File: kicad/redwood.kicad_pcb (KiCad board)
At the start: 2 copper layers, 136.6 x 97.9 mm, 39 parts, among them J1 Haptic, J2 TRRS, K1 diode-choc, K10 diode-choc, K11 diode-choc, K12 diode-choc, K13 diode-choc, K14 diode-choc, K15 diode-choc, K16 diode-choc, K17 diode-choc, K18 diode-choc, K19 diode-choc, K2 diode-choc, K20 choc_rotary, K21 diode-choc, K22 diode-choc, K23 diode-choc, K24 diode-choc, K3 diode-choc, K4 diode-choc, K5 diode-choc, K6 diode-choc, K7 diode-choc, K8 diode-choc, K9 diode-choc, SW1 Reset, U1 ProMicro_r

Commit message: - project updates from footprints
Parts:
- added V2: Via, mmccoyd:VIA-0.8mm, F.Cu at (182.0, 85.7)
- moved J1 0.50 mm to (215.5, 93.5)
- moved J2 0.50 mm to (214.5, 129.4)
- moved R1 0.50 mm to (221.1, 90.4)
- moved R2 0.50 mm to (221.1, 80.0)
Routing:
- net VCC: track 224.7 -> 225.9 mm
- net col1: track 196.3 -> 195.5 mm
- net SCL: track 41.6 -> 42.1 mm
- net SDA: track 42.3 -> 42.8 mm
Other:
- outline, holes or cut-outs redrawn

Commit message: Symbols and footprints all from project libs
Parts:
- V1, V2: footprint mmccoyd:VIA-0.8mm -> redwood:VIA-0.8mm

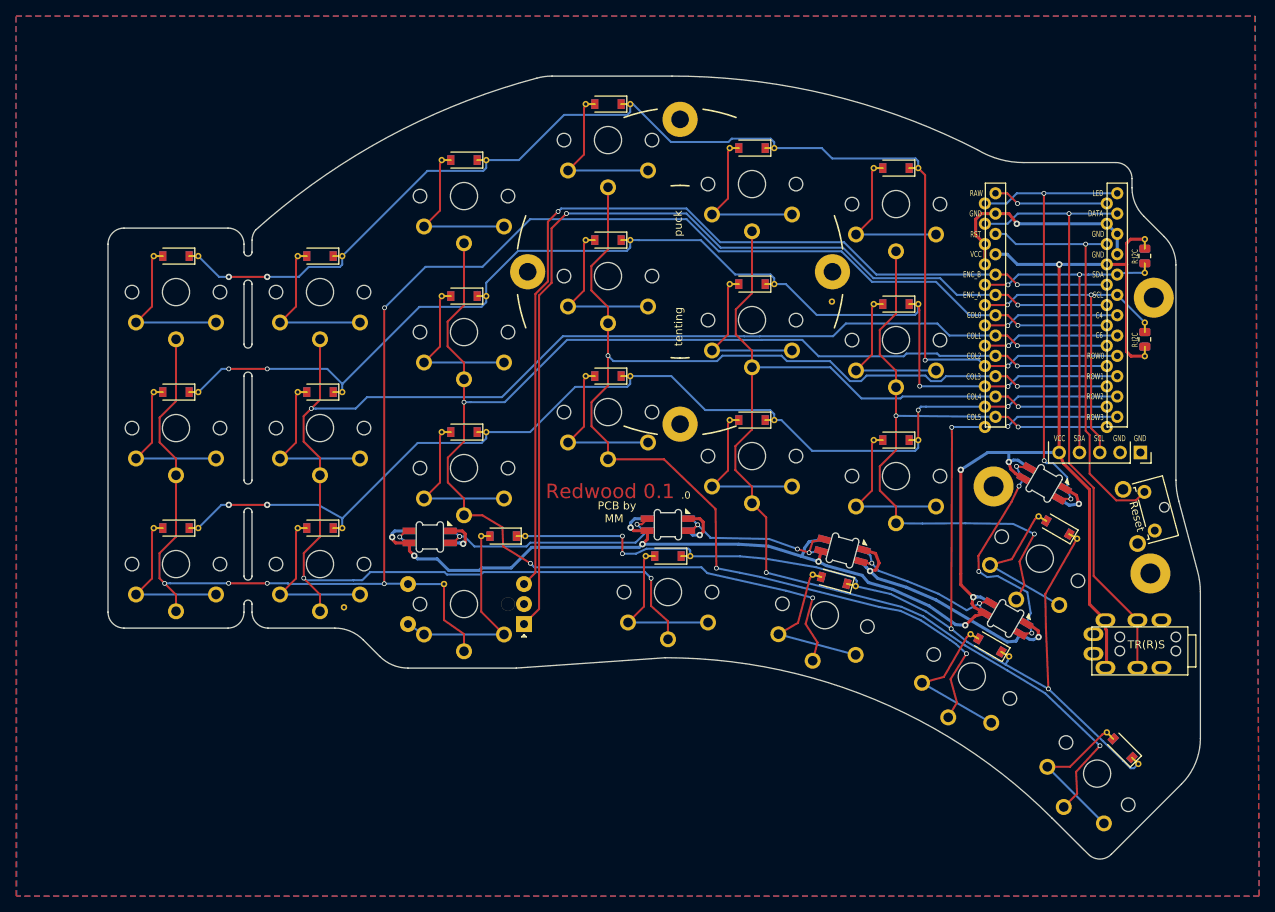
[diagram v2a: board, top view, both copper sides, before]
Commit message: Common cathode diodes reduce trace clutter
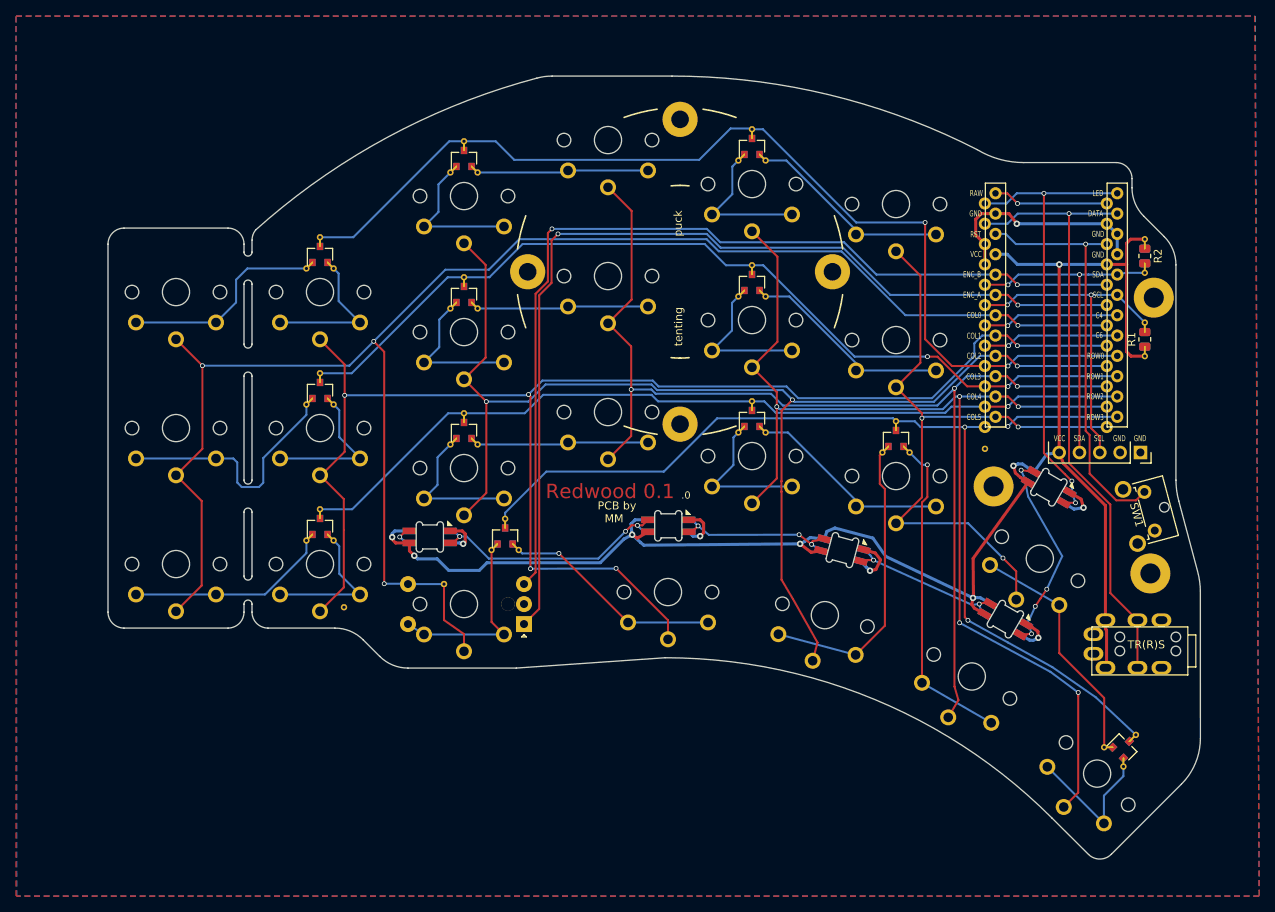
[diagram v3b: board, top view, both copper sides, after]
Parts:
- removed D6: Diode, redwood:D_SOD-123_rev
- added D10: BAV70, ki_syms:SOT-23, F.Cu at (118.0, 96.8)
- added D11: BAV70, ki_syms:SOT-23, F.Cu at (136.0, 84.8)
- added D12: BAV70, ki_syms:SOT-23, F.Cu at (172.0, 83.3)
- added D13: BAV70, ki_syms:SOT-23, F.Cu at (118.0, 113.8)
- added D14: BAV70, ki_syms:SOT-23, F.Cu at (136.0, 101.8)
- added D15: BAV70, ki_syms:SOT-23, F.Cu at (172.0, 100.3)
- added D16: BAV70, ki_syms:SOT-23, F.Cu at (141.1, 115.0)
- added D17: BAV70, ki_syms:SOT-23, F.Cu at (190.0, 102.8)
- added D18: BAV70, ki_syms:SOT-23, F.Cu at (218.5, 141.4)
- added D7: BAV70, ki_syms:SOT-23, F.Cu at (118.0, 79.8)
- added D8: BAV70, ki_syms:SOT-23, F.Cu at (136.0, 67.8)
- added D9: BAV70, ki_syms:SOT-23, F.Cu at (172.0, 66.3)
- D1, D2, D3, D4, D5: footprint redwood:SK6812-MINI-E -> ki_syms:SK6812-MINI-E
- K1, K10, K11, K12, K13, K14, K15, K16, K17, K18, K19, K2, K21, K22, K23, K24, K3, K4, K5, K6, K7, K8, K9: value diode-choc -> SW_Key; footprint redwood:pg1350-DR -> redwood:pg1350-R
- K20: value choc_rotary -> SW_Rotary
- R1, R2: footprint redwood:R_0805_2012Metric -> ki_syms:R_0805_2012Metric
- SW1: footprint redwood:SW_Tactile_SPST_Angled_MJTP1117 -> ki_syms:SW_Tactile_SPST_Angled_MJTP1117
- V1, V2: footprint redwood:VIA-0.8mm -> ki_syms:VIA-0.8mm
- moved V2 26.5 mm to (201.1, 104.1)
- moved K1 4.50 mm to (100.0, 84.5)
- moved K10 4.50 mm to (154.0, 82.5)
- moved K11 4.50 mm to (172.0, 88.0)
- moved K12 4.50 mm to (190.0, 90.5)
- moved K13 4.50 mm to (100.0, 118.5)
- moved K14 4.50 mm to (118.0, 118.5)
- moved K15 4.50 mm to (136.0, 106.5)
- moved K16 4.50 mm to (154.0, 99.5)
- moved K17 4.50 mm to (172.0, 105.0)
- moved K18 4.50 mm to (190.0, 107.5)
- moved K2 4.50 mm to (118.0, 84.5)
- moved K21 4.50 mm to (161.5, 122.0)
- moved K3 4.50 mm to (136.0, 72.5)
- moved K4 4.50 mm to (154.0, 65.5)
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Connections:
- K1 pad 2: row0 -> Net-(D7-Pad1)
- K10 pad 2: row1 -> Net-(D11-Pad2)
- K11 pad 2: row1 -> Net-(D12-Pad1)
- K12 pad 2: row1 -> Net-(D12-Pad2)
- K13 pad 2: row2 -> Net-(D13-Pad1)
- K14 pad 2: row2 -> Net-(D13-Pad2)
- K15 pad 2: row2 -> Net-(D14-Pad1)
- K16 pad 2: row2 -> Net-(D14-Pad2)
- K17 pad 2: row2 -> Net-(D15-Pad1)
- K18 pad 2: row2 -> Net-(D15-Pad2)
- K19 pad 2: row3 -> Net-(D18-Pad1)
- K2 pad 2: row0 -> Net-(D7-Pad2)
- K21 pad 2: row3 -> Net-(D16-Pad2)
- K22 pad 2: row3 -> Net-(D17-Pad1)
- K23 pad 2: row3 -> Net-(D17-Pad2)
- K24 pad 2: row3 -> Net-(D18-Pad2)
- K3 pad 2: row0 -> Net-(D8-Pad1)
- K4 pad 2: row0 -> Net-(D8-Pad2)
- K5 pad 2: row0 -> Net-(D9-Pad1)
- K6 pad 2: row0 -> Net-(D9-Pad2)
- K7 pad 2: row1 -> Net-(D10-Pad1)
- K8 pad 2: row1 -> Net-(D10-Pad2)
- K9 pad 2: row1 -> Net-(D11-Pad1)
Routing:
- net Net-(D17-Pad2): track 0.00 -> 30.4 mm, vias 0 -> 1
- net row1: track 143.9 -> 114.3 mm, vias 4 -> 2
- net row2: track 136.0 -> 107.4 mm, vias 4 -> 1
- net row0: track 156.8 -> 128.6 mm, vias 4 -> 2
- net Net-(D17-Pad1): track 0.00 -> 27.2 mm
- net col3: track 168.8 -> 142.7 mm, vias 4 -> 3
- net col2: track 178.9 -> 155.3 mm, vias 4 -> 3
- net row3: track 156.1 -> 133.0 mm, vias 6 -> 3
- net GND: track 76.8 -> 55.4 mm
- net Net-(D10-Pad1): track 0.00 -> 21.1 mm
- net Net-(D18-Pad1): track 0.00 -> 20.1 mm
- net Net-(D16-Pad2): track 0.00 -> 17.4 mm, vias 0 -> 1
- net Net-(D7-Pad1): track 0.00 -> 15.7 mm
- net Net-(D12-Pad2): track 0.00 -> 15.7 mm
- net Net-(D15-Pad2): track 0.00 -> 15.6 mm
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
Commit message: Battery support, Hillside logo, mounting holes
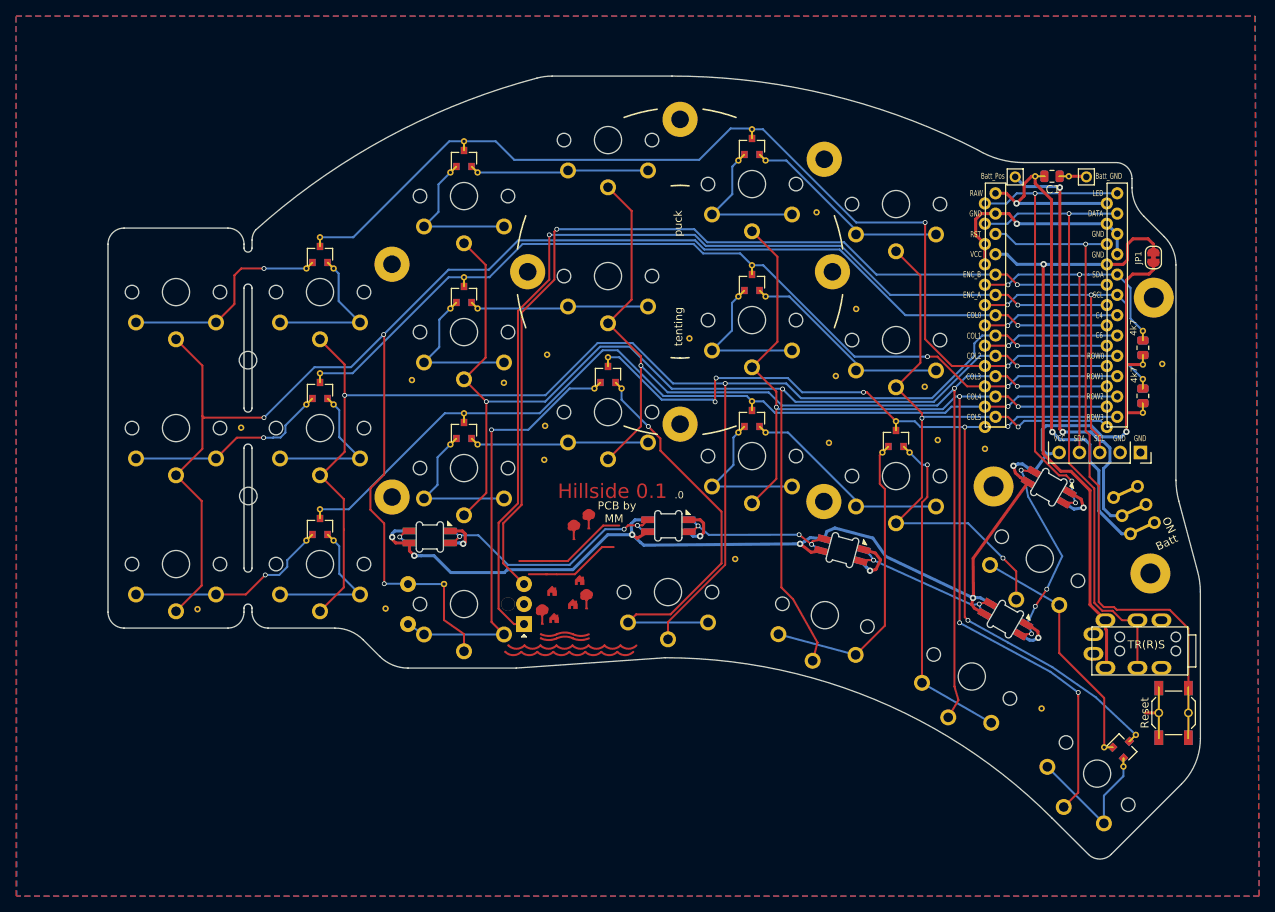
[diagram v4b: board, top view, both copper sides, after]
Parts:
- added C1: 4u7, ki_syms:C_0805_2012Metric, F.Cu at (209.5, 70.0)
- added H3: Scene, redwood:Hillside_Scene, F.Cu at (149.1, 121.4)
- added H4: MountHole, ki_mount_hole:MountingHole_2.2mm_M2_Pad, F.Cu at (127.0, 81.0)
- added H5: MountHole, ki_mount_hole:MountingHole_2.2mm_M2_Pad, F.Cu at (127.0, 110.1)
- added H6: MountHole, ki_mount_hole:MountingHole_2.2mm_M2, F.Cu at (109.0, 93.0)
- added H7: MountHole, ki_mount_hole:MountingHole_2.2mm_M2, F.Cu at (109.0, 110.0)
- added H8: MountHole, ki_mount_hole:MountingHole_2.2mm_M2_Pad, F.Cu at (181.0, 110.7)
- added H9: MountHole, ki_mount_hole:MountingHole_2.2mm_M2_Pad, F.Cu at (181.0, 67.9)
- added J3: Batt_Pos, ki_syms:1pin_conn, F.Cu at (204.9, 70.1)
- added J4: Batt_GND, ki_syms:1pin_conn, F.Cu at (213.8, 70.1)
- added JP1: SolderJumper_2_Bridged, ki_syms:SolderJumper-2_P1.3mm_Bridged_RoundedPad1.0x1.5mm, F.Cu at (222.2, 80.2)
- added SW2: SW_Power, ki_syms:SW_SPDT_JS202011AQN, F.Cu at (219.8, 111.8)
- added V10: Via, ki_syms:VIA-0.8mm, F.Cu at (146.1, 101.2)
- added V11: Via, ki_syms:VIA-0.8mm, F.Cu at (182.5, 95.0)
- added V12: Via, ki_syms:VIA-0.8mm, F.Cu at (164.2, 90.3)
- added V13: Via, ki_syms:VIA-0.8mm, F.Cu at (129.5, 95.5)
- added V14: Via, ki_syms:VIA-0.8mm, F.Cu at (185.0, 86.6)
- added V15: Via, ki_syms:VIA-0.8mm, F.Cu at (102.7, 124.1)
- added V16: Via, ki_syms:VIA-0.8mm, F.Cu at (108.1, 101.5)
- added V17: Via, ki_syms:VIA-0.8mm, F.Cu at (195.2, 103.0)
- added V18: Via, ki_syms:VIA-0.8mm, F.Cu at (193.6, 96.3)
- added V19: Via, ki_syms:VIA-0.8mm, F.Cu at (141.0, 95.8)
- added V3: Via, ki_syms:VIA-0.8mm, F.Cu at (223.3, 93.5)
- added V4: Via, ki_syms:VIA-0.8mm, F.Cu at (208.2, 136.6)
- added V5: Via, ki_syms:VIA-0.8mm, F.Cu at (169.9, 117.9)
- added V6: Via, ki_syms:VIA-0.8mm, F.Cu at (126.2, 124.1)
- added V7: Via, ki_syms:VIA-0.8mm, F.Cu at (146.4, 92.3)
- added V8: Via, ki_syms:VIA-0.8mm, F.Cu at (146.0, 105.5)
- added V9: Via, ki_syms:VIA-0.8mm, F.Cu at (181.6, 103.3)
- H1: value Tenting_Mount -> Mount_Tenting
- R1, R2: value R:I2C -> 4k7
- SW1: footprint ki_syms:SW_Tactile_SPST_Angled_MJTP1117 -> ki_syms:SW_SPST_SKQG_WithStem
- V1: value Via -> V
- moved V1 77.0 mm to (180.1, 74.5)
- moved SW1 27.9 mm to (224.7, 137.1), turned to 270 degrees
- moved D16 23.9 mm to (154.0, 94.8)
- moved R2 11.5 mm to (220.9, 91.5), turned to 90 degrees
- moved R1 7.07 mm to (220.9, 97.5)
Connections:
- D1 pad 1: VCC -> VCC_ACC
- D2 pad 1: VCC -> VCC_ACC
- D3 pad 1: VCC -> VCC_ACC
- D4 pad 1: VCC -> VCC_ACC
- D5 pad 1: VCC -> VCC_ACC
- J1 pad 5: VCC -> VCC_ACC
- R1 pad 1: VCC -> VCC_ACC
- R2 pad 1: VCC -> VCC_ACC
- U1 pad 24: Net-(U1-Pad24) -> raw
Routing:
- net VCC_ACC: track 0.00 -> 167.3 mm, vias 0 -> 7
- net VCC: track 212.7 -> 78.8 mm, vias 7 -> 1
- net raw: track 0.00 -> 71.1 mm, vias 0 -> 2
- net bat+: track 0.00 -> 54.7 mm, vias 0 -> 2
- net Net-(D16-Pad1): track 11.2 -> 41.2 mm, vias 0 -> 1
- net reset: track 52.0 -> 79.9 mm
- net Net-(D16-Pad2): track 17.4 -> 41.8 mm
- net Net-(U1-Pad24): track 14.4 -> 0.00 mm, vias 1 -> 0
- net row3: track 133.0 -> 122.3 mm, vias 3 -> 6
- net SCL: track 42.1 -> 49.1 mm
- net Net-(D10-Pad1): track 21.1 -> 14.6 mm, vias 0 -> 1
- net col1: track 184.7 -> 179.4 mm, vias 5 -> 3
- net col2: track 155.3 -> 160.2 mm
- net SDA: track 42.8 -> 47.7 mm
- net row2: track 107.4 -> 112.0 mm
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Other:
- outline, holes or cut-outs redrawn
- board text added: "Hillside 0.1"
- board text removed: "Redwood 0.1"
